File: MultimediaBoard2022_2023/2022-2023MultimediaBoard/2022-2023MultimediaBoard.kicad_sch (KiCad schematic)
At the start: 21 parts

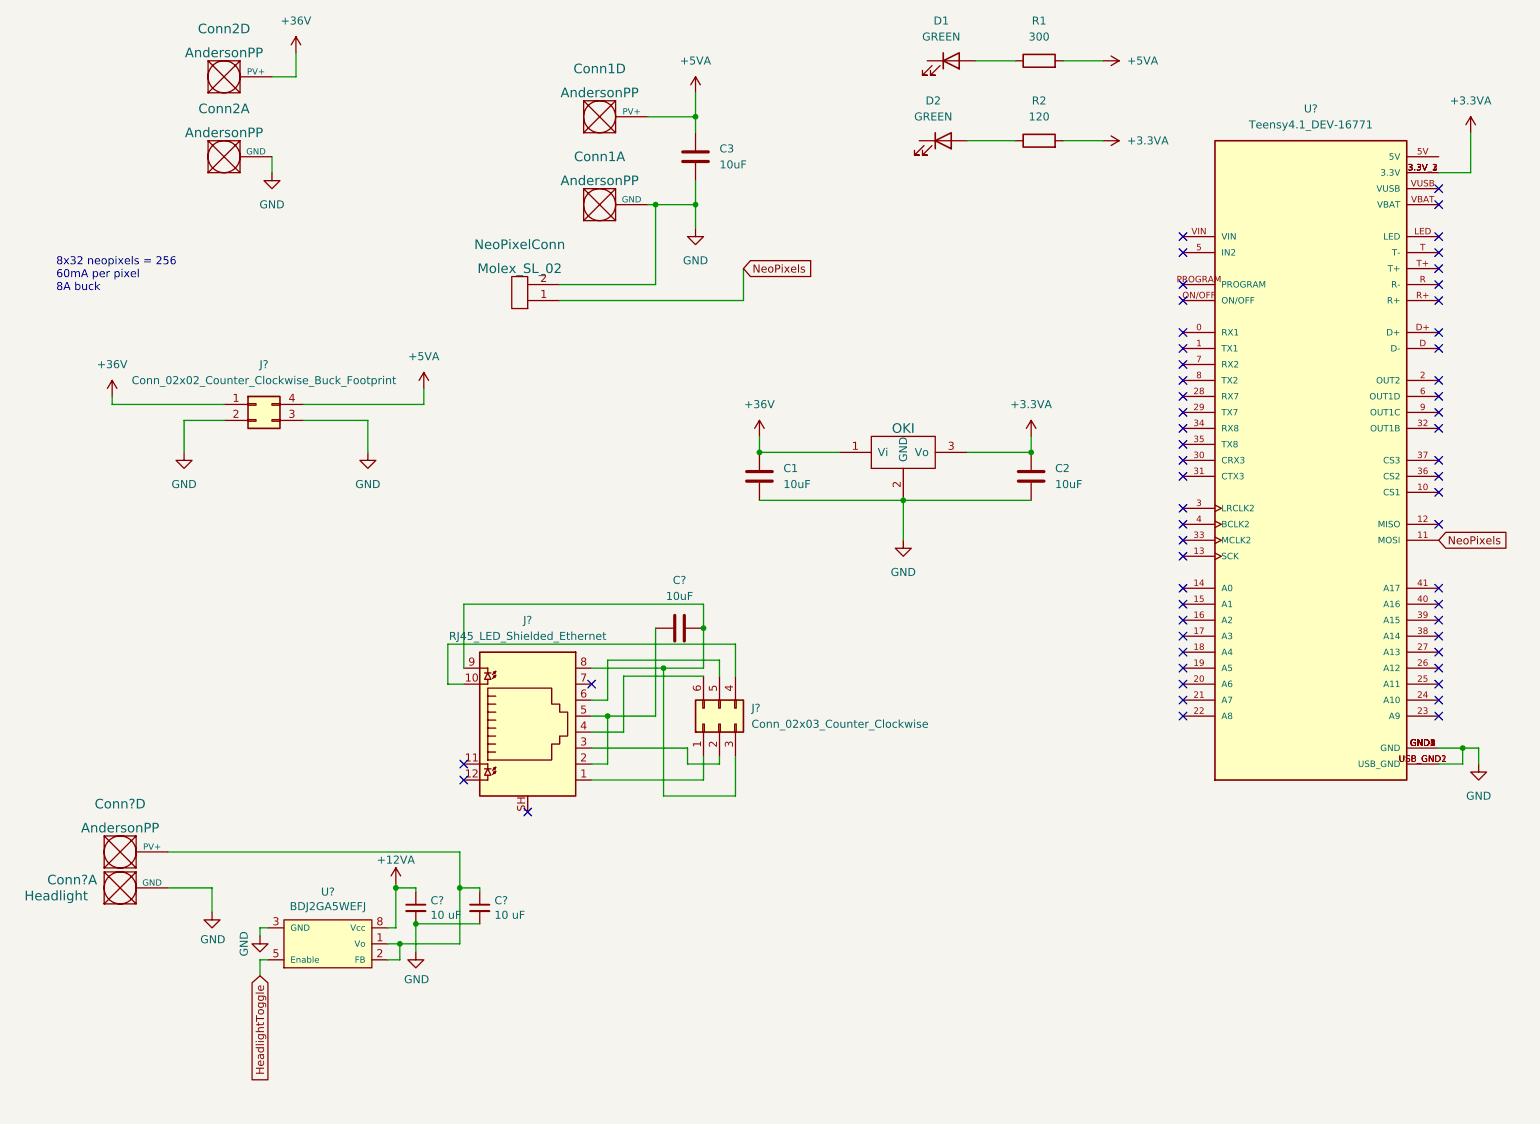
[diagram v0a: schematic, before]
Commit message: removed headlight components
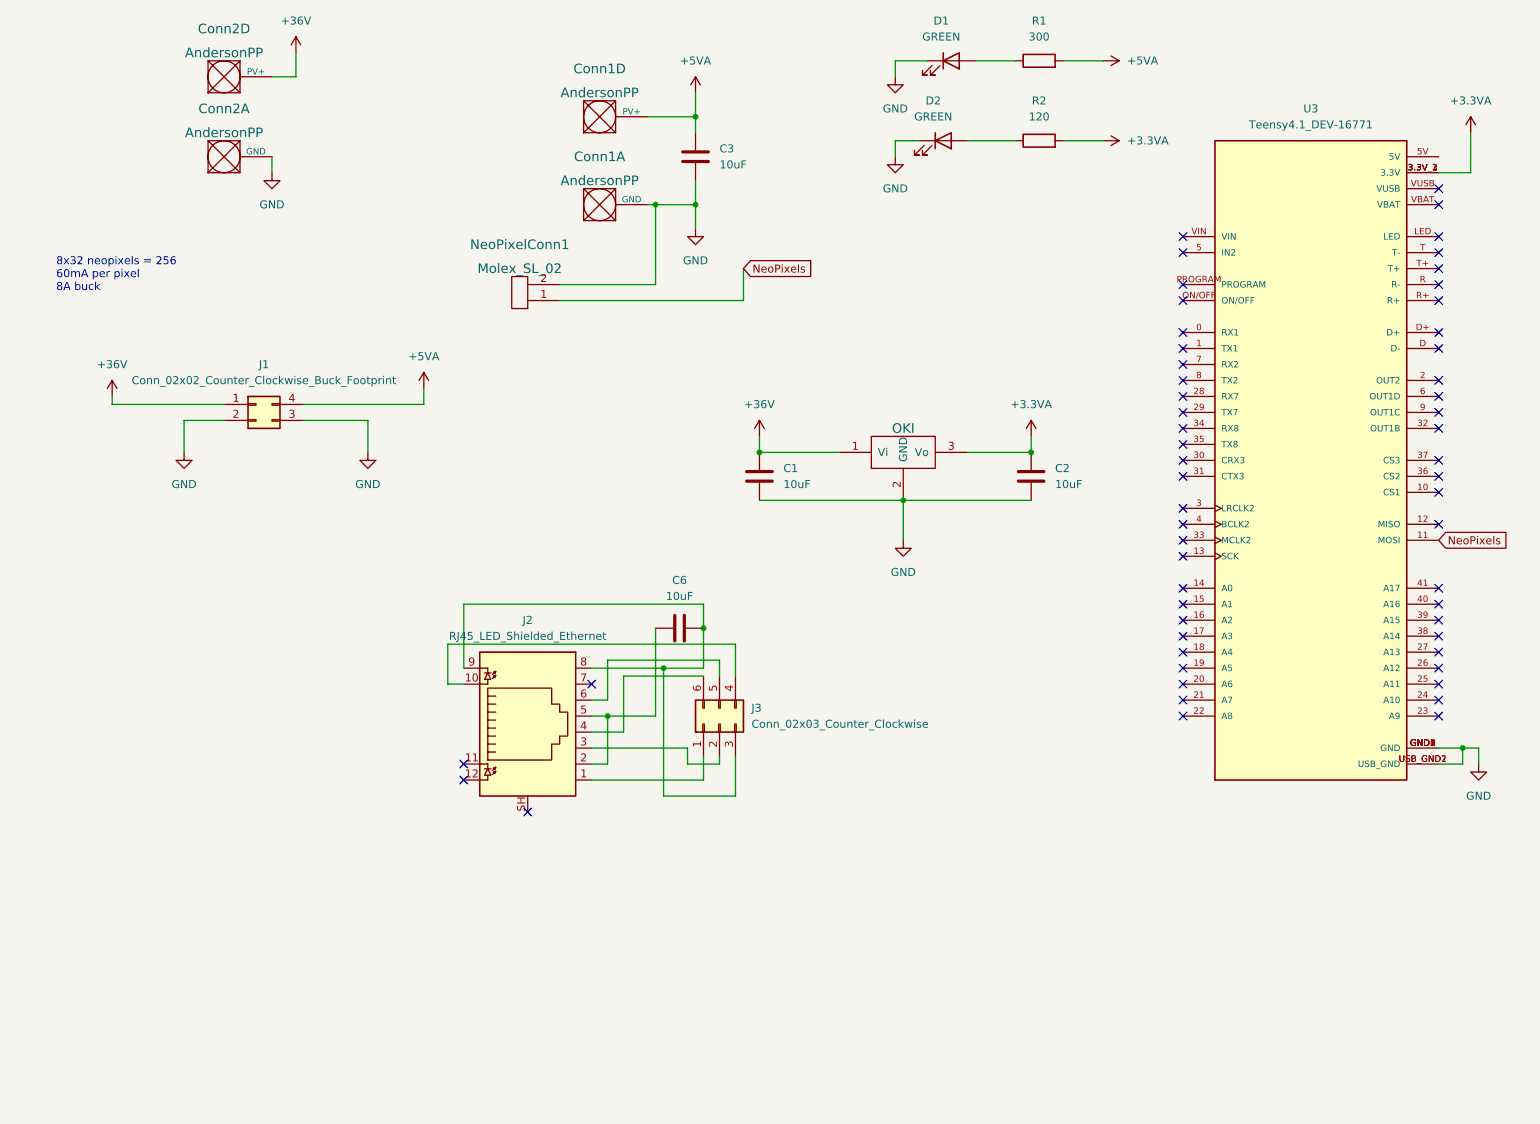
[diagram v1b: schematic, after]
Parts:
- removed C? (x2): 10 uF, Capacitor_SMD:C_0603_1608Metric_Pad1.05x0.95mm_HandSolder, symbol Device:C_Small
- removed Conn?: Headlight, MRDT_Connectors:Square_Anderson_2_H_Side_By_Side, symbol MRDT_Connectors:AndersonPP
- removed Conn?: AndersonPP, symbol MRDT_Connectors:AndersonPP
- removed U?: BDJ2GA5WEFJ, Package_SO:SOIC-8-1EP_3.9x4.9mm_P1.27mm_EP2.29x3mm, symbol Multimedia_IC:BDJ2GA5WEFJ
- C1, C2, C3: footprint (none) -> Capacitor_SMD:C_0603_1608Metric_Pad1.08x0.95mm_HandSolder
- C6: renamed from C?; footprint (none) -> Capacitor_SMD:C_0603_1608Metric_Pad1.08x0.95mm_HandSolder
- Conn1, Conn2: footprint (none) -> MRDT_Connectors:Square_Anderson_2_H_Side_By_Side_PV
- D1, D2: footprint (none) -> LED_SMD:LED_0603_1608Metric_Pad1.05x0.95mm_HandSolder
- J1: renamed from J?; footprint (none) -> Connector_PinHeader_2.00mm:PinHeader_2x02_P2.00mm_Vertical
- J2: renamed from J?; footprint (none) -> MRDT_Connectors:RJ45_Teensy
- J3: renamed from J?; footprint (none) -> Connector_PinHeader_2.00mm:PinHeader_2x03_P2.00mm_Vertical
- NeoPixelConn1: renamed from NeoPixelConn; footprint (none) -> MRDT_Connectors:MOLEX_SL_02_Horizontal
- R1, R2: footprint (none) -> Resistor_SMD:R_0201_0603Metric_Pad0.64x0.40mm_HandSolder
- U2: renamed from U?; footprint (none) -> MRDT_Devices:OKI_Horizontal
- U3: renamed from U?; footprint MODULE_DEV-16771 -> MRDT_Shields:MODULE_DEV-16771
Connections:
- net GND: now also D1.1 (K), D2.1 (K)
